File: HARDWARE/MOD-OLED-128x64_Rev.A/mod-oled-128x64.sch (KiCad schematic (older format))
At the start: 13 parts, among them P1 n.a.

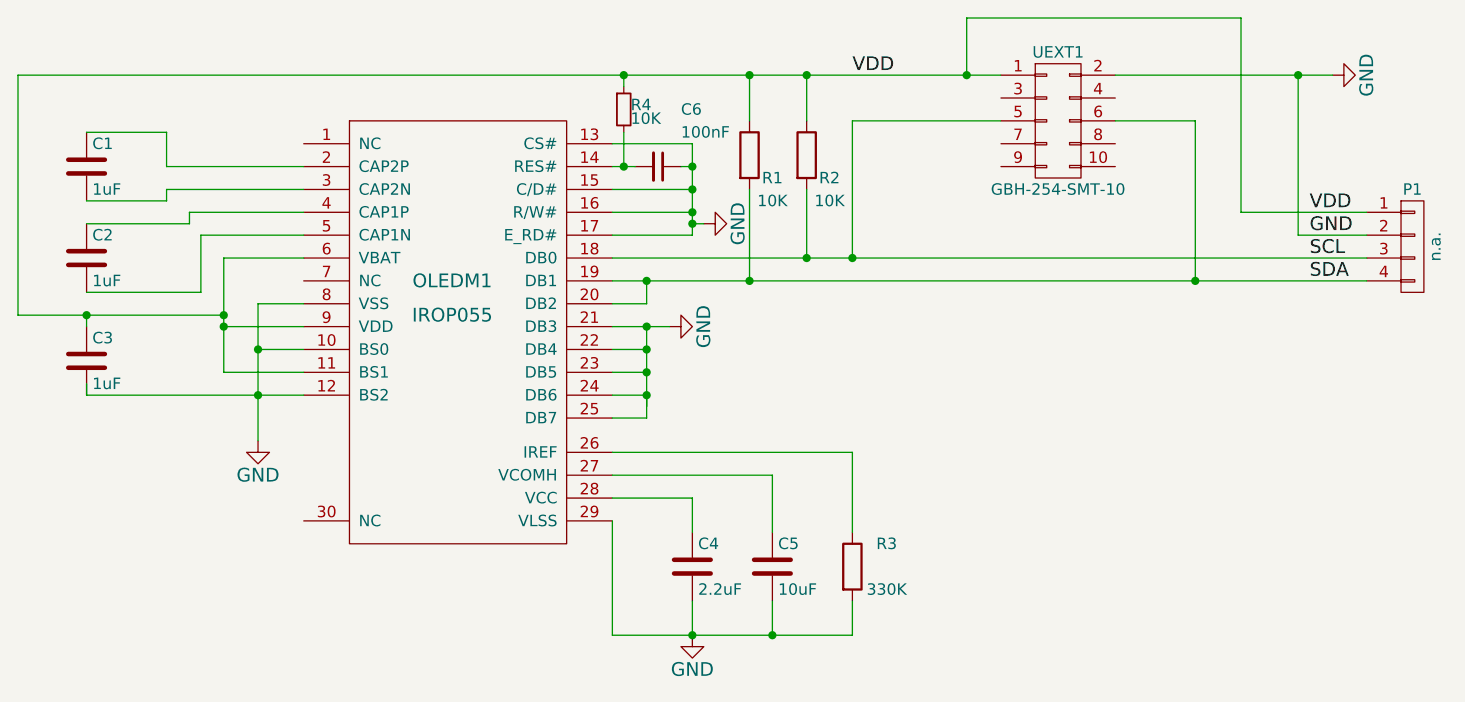
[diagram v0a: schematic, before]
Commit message: All GND symbols should point down
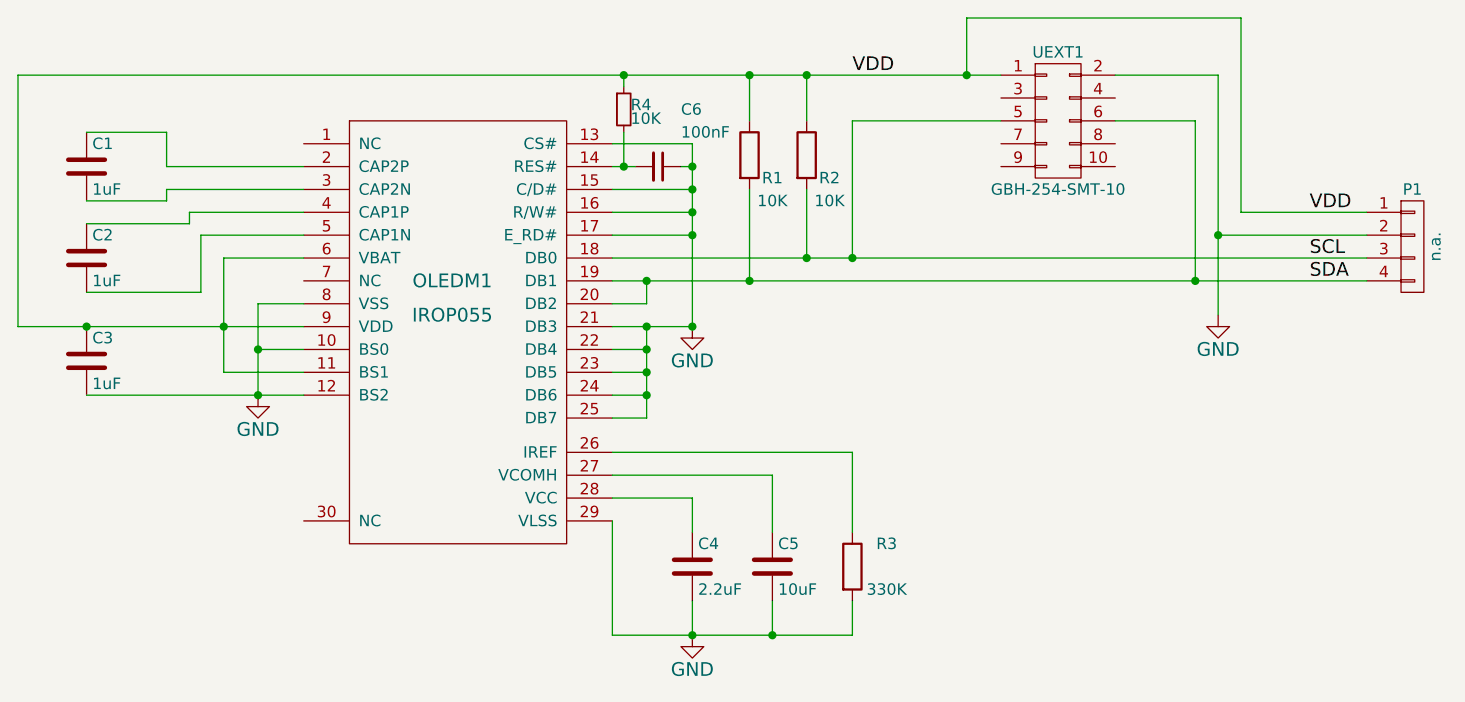
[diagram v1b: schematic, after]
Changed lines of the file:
@@
 	3250 2750 3250 3250
 Wire Wire Line
-	3250 3050 3600 3050
-Connection ~ 3250 3000
+	2350 3050 3600 3050
 Wire Wire Line
 	3250 3250 3600 3250
@@
 Connection ~ 3400 3150
 Wire Wire Line
-	3400 2950 3400 3550
+	3400 2950 3400 3350
 Wire Wire Line
 	2650 3350 3600 3350
 Connection ~ 3400 3350
-Wire Wire Line
-	2650 3300 2650 3350
 $Comp
 L GND #PWR01
 U 1 1 54FFFAD7
-P 3400 3550
-F 0 "#PWR01" H 3400 3300 60  0001 C CNN
-F 1 "GND" H 3400 3400 60  0000 C CNN
-F 2 "" H 3400 3550 60  0000 C CNN
-F 3 "" H 3400 3550 60  0000 C CNN
-	1    3400 3550
+P 3400 3350
+F 0 "#PWR01" H 3400 3100 60  0001 C CNN
+F 1 "GND" H 3400 3200 60  0000 C CNN
+F 2 "" H 3400 3350 60  0000 C CNN
+F 3 "" H 3400 3350 60  0000 C CNN
+	1    3400 3350
 	1    0    0    -1
 $EndComp
@@
 $EndComp
 Wire Wire Line
-	2650 3000 2650 3050
-Wire Wire Line
-	6650 1950 2350 1950
-Wire Wire Line
-	2350 1950 2350 3000
-Wire Wire Line
-	2350 3000 3250 3000
+	2350 1950 6650 1950
 Text Label 6000 1950 0    60   ~ 0
 VDD
@@
 Connection ~ 5100 2850
 Wire Wire Line
-	4950 3050 5200 3050
+	5300 3050 4950 3050
 Wire Wire Line
 	5100 3050 5100 3450
 Wire Wire Line
-	5100 3450 4950 3450
-Connection ~ 5100 3050
-Wire Wire Line
-	4950 3350 5100 3350
-Wire Wire Line
-	5100 3350 5100 3400
-Connection ~ 5100 3350
+	5100 3350 4950 3350
 Wire Wire Line
 	4950 3250 5100 3250
@@
 $Comp
 L GND #PWR02
-U 1 1 5500011D
-P 5200 3050
-F 0 "#PWR02" H 5200 2800 60  0001 C CNN
-F 1 "GND" H 5200 2900 60  0000 C CNN
-F 2 "" H 5200 3050 60  0000 C CNN
-F 3 "" H 5200 3050 60  0000 C CNN
-	1    5200 3050
-	0    -1   -1   0
-$EndComp
-$Comp
-L GND #PWR03
 U 1 1 55000254
-P 5350 2600
-F 0 "#PWR03" H 5350 2350 60  0001 C CNN
-F 1 "GND" H 5350 2450 60  0000 C CNN
-F 2 "" H 5350 2600 60  0000 C CNN
-F 3 "" H 5350 2600 60  0000 C CNN
-	1    5350 2600
-	0    -1   -1   0
+P 5300 3050
+F 0 "#PWR02" H 5300 2800 60  0001 C CNN
+F 1 "GND" H 5300 2900 60  0000 C CNN
+F 2 "" H 5300 3050 60  0000 C CNN
+F 3 "" H 5300 3050 60  0000 C CNN
+	1    5300 3050
+	1    0    0    -1
 $EndComp
 $Comp
@@
 	6000 3600 6000 3950
 Wire Wire Line
-	6000 4250 6000 4400
-Wire Wire Line
-	6000 4400 4950 4400
+	6000 4400 6000 4250
+Wire Wire Line
+	4950 4400 6000 4400
 Wire Wire Line
 	4950 4400 4950 3900
@@
 Connection ~ 5650 4400
 $Comp
-L GND #PWR04
+L GND #PWR03
 U 1 1 55000734
 P 5300 4400
-F 0 "#PWR04" H 5300 4150 60  0001 C CNN
+F 0 "#PWR03" H 5300 4150 60  0001 C CNN
 F 1 "GND" H 5300 4250 60  0000 C CNN
 F 2 "" H 5300 4400 60  0000 C CNN
@@
 $EndComp
 Wire Wire Line
-	7150 1950 8100 1950
+	7150 1950 7600 1950
+Wire Wire Line
+	7600 1950 7600 3000
 Wire Wire Line
 	6500 1950 6500 1700
@@
 Connection ~ 6000 2750
 $Comp
-L GND #PWR05
+L GND #PWR04
 U 1 1 550012EF
-P 8100 1950
-F 0 "#PWR05" H 8100 1700 60  0001 C CNN
-F 1 "GND" H 8100 1800 60  0000 C CNN
-F 2 "" H 8100 1950 60  0000 C CNN
-F 3 "" H 8100 1950 60  0000 C CNN
-	1    8100 1950
-	0    -1   -1   0
-$EndComp
-Connection ~ 7950 1950
-Text Label 8000 2650 0    60   ~ 0
-GND
+P 7600 3000
+F 0 "#PWR04" H 7600 2750 60  0001 C CNN
+F 1 "GND" H 7600 2850 60  0000 C CNN
+F 2 "" H 7600 3000 60  0000 C CNN
+F 3 "" H 7600 3000 60  0000 C CNN
+	1    7600 3000
+	1    0    0    -1
+$EndComp
 Text Label 8000 2550 0    60   ~ 0
 VDD
@@
 Text Label 8000 2750 0    60   ~ 0
 SCL
-Wire Wire Line
-	7950 1950 7950 2650
 Wire Wire Line
 	7700 1700 7700 2550
@@
 $EndComp
 Wire Wire Line
-	7950 2650 8250 2650
-Wire Wire Line
 	7700 2550 8250 2550
-Connection ~ 2650 3000
 $Comp
 L C_Small C6
@@
 Wire Wire Line
 	5000 1950 5000 2000
-Connection ~ 5000 1950
 Wire Wire Line
 	5000 2200 5000 2350
@@
 	4950 2250 5300 2250
 Wire Wire Line
-	5300 2250 5300 2650
-Wire Wire Line
 	5300 2650 4950 2650
 Connection ~ 5300 2350
 Wire Wire Line
-	4950 2550 5300 2550
+	5300 2550 4950 2550
+Wire Wire Line
+	5300 2450 4950 2450
+Connection ~ 5300 2450
+Wire Wire Line
+	5300 2250 5300 3050
+Connection ~ 5300 3050
+Connection ~ 5100 3050
+Connection ~ 5300 2650
 Connection ~ 5300 2550
 Wire Wire Line
-	4950 2450 5300 2450
-Connection ~ 5300 2450
-Wire Wire Line
-	5300 2600 5350 2600
-Connection ~ 5300 2600
+	5100 3450 4950 3450
+Connection ~ 5100 3350
+Wire Wire Line
+	8250 2650 7600 2650
+Connection ~ 7600 2650
+Connection ~ 5000 1950
+Wire Wire Line
+	2350 1950 2350 3050
+Connection ~ 2650 3050
 $EndSCHEMATC
